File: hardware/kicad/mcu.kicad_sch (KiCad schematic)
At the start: 38 parts, among them J101 TC2050-IDC-NL, J102 UART (TX RX GND), SW101 BOOT, U101 STM32F469IIT6, Y101 8MHz CL10pF, Y102 32.768kHz CL6pF

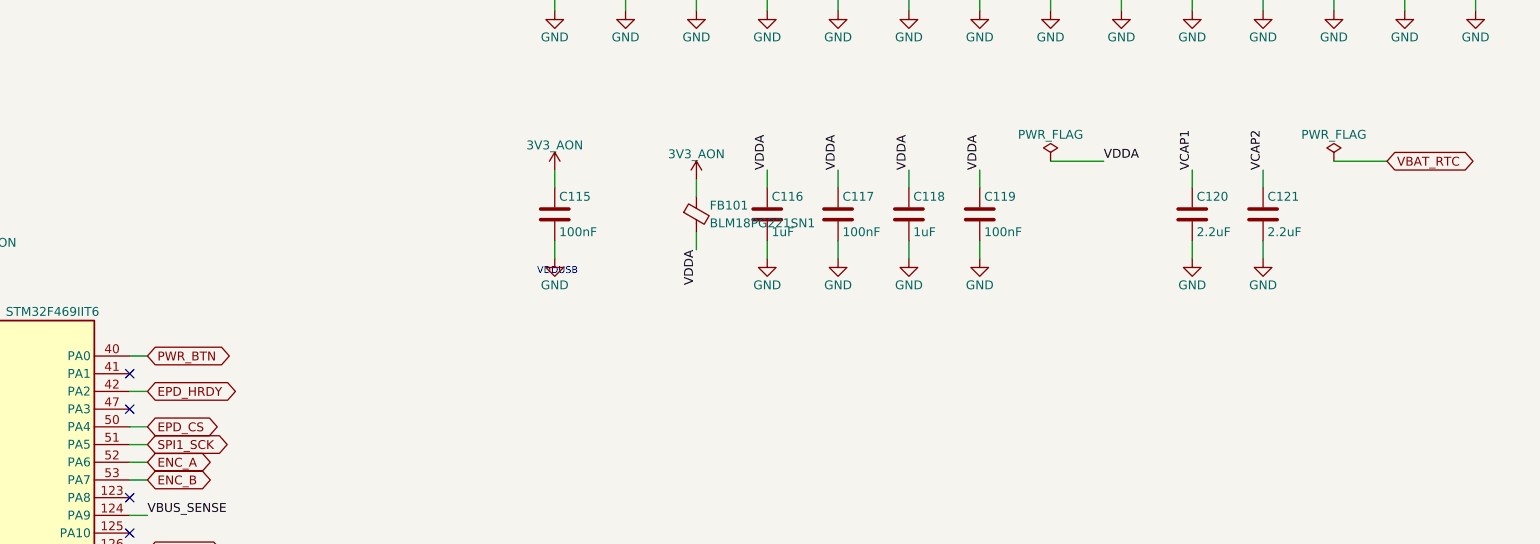
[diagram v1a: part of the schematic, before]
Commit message: Switch battery chemistry from LiFePO4 to 1-cell LiPo pouch
Small flat LFP pouches aren't practically buyable in the US; protected LiPo
pouches with JST-PH leads are stocked everywhere.

Power sheet:
- MCP73123 (3.6 V LFP) + discrete AN1149 load sharing (D1/Q1/R5) ->
  TI BQ24073: 4.2 V CV, power path with OUT (VSYS) regulated to 4.4 V so
  the 5.5 V-max TPS63802/TPS61023 stay safe, USB500 input limit, ~500 mA
  charge (ISET 1.78k), ILIM 1.54k fitted (open ILIM disables charging),
  on-board 10k NTC on TS (0-50 C charge window).
- RTC backup: BAT54J -> MCP1700 3.0 V LDO (4.2 V minus a diode drop would
  exceed VBAT's 3.6 V max).
- New VBAT_SENSE 1M/1M divider to PA3 (ADC1_IN3) for the firmware cutoff and
  fuel estimate (VBAT_RTC is now clamped by the LDO).
- UVLO divider on TPS63802 EN 1.8M/1M -> 2.2M/1M (off ~3.20 V, on ~3.52 V).
- MCP73123 project symbol removed; redundant VBAT_RTC PWR_FLAG removed.

README/TODO: chemistry rationale and trade-offs, new power tree, battery
protection layers, updated sheet notes and open items (cell choice, NTC
coupling, fitting the peripheral load switch on v1).

ERC 0 violations; check_schematic.py OK (190 nets, 84 MCU pins, 38 power-
sheet nets); PA3 pin number cross-checked against DS11189.

Co-Authored-By: Claude Opus 5.5 <noreply@anthropic.com>
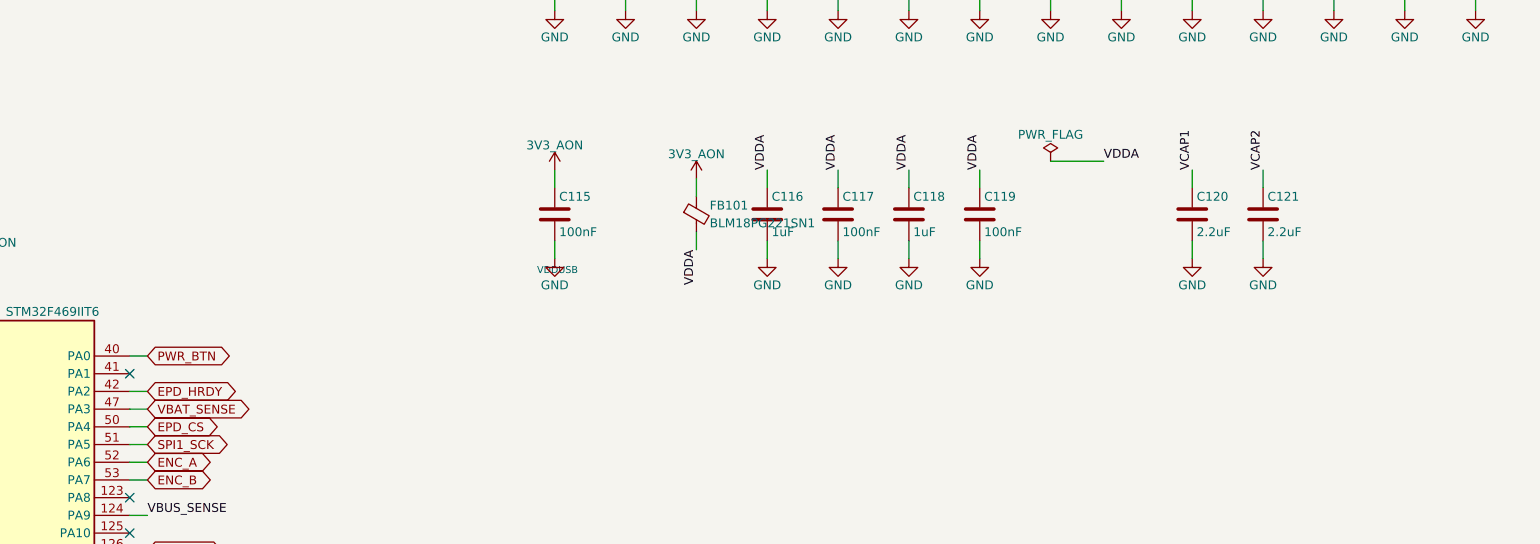
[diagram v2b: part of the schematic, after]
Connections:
- net VBAT_SENSE: now reaches U101.47 (PA3)
- no-connect marks 56 -> 55
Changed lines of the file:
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@@
 	(wire
 		(pts
+			(xy 340.36 124.46)
+			(xy 342.9 124.46)
+		)
+		(stroke
+			(width 0)
+			(type default)
+		)
+	)
+	(global_label "VBAT_SENSE"
+		(shape bidirectional)
+		(at 342.9 124.46 0)
+		(fields_autoplaced yes)
+		(effects
+			(font
+				(size 1.27 1.27)
+			)
+			(justify left)
+		)
+		(property "Intersheetrefs" "${INTERSHEET_REFS}"
+			(at 342.9 124.46 0)
+			(hide yes)
+			(effects
+				(font
+					(size 1.27 1.27)
+				)
+				(justify left)
+			)
+		)
+	)
+	(wire
+		(pts
 			(xy 254 223.52)
 			(xy 251.46 223.52)
@@
 	)
 	(no_connect
-		(at 340.36 124.46)
-	)
-	(no_connect
 		(at 340.36 213.36)
 	)
@@
 		)
 	)
-	(symbol
-		(lib_id "power:PWR_FLAG")
-		(at 513.08 88.9 0)
-		(unit 1)
-		(exclude_from_sim no)
-		(in_bom no)
-		(on_board yes)
-		(dnp no)
-		(property "Reference" "#FLGMCU49"
-			(at 513.08 86.995 0)
-			(hide yes)
-			(effects
-				(font
-					(size 1.27 1.27)
-				)
-			)
-		)
-		(property "Value" "PWR_FLAG"
-			(at 513.08 85.09 0)
-			(effects
-				(font
-					(size 1.27 1.27)
-				)
-			)
-		)
-		(property "Footprint" ""
-			(at 513.08 88.9 0)
-			(hide yes)
-			(effects
-				(font
-					(size 1.27 1.27)
-				)
-			)
-		)
-		(property "Datasheet" ""
-			(at 513.08 88.9 0)
-			(hide yes)
-			(effects
-				(font
-					(size 1.27 1.27)
-				)
-			)
-		)
-		(property "Description" "Special symbol for telling ERC where power comes from"
-			(at 513.08 88.9 0)
-			(hide yes)
-			(effects
-				(font
-					(size 1.27 1.27)
-				)
-			)
-		)
-		(pin "1"
-		)
-		(instances
-			(project "stm32-epaper"
-				(path "/6f1d3c2a-5b7e-4c1d-9a0f-000000000001/6f1d3c2a-5b7e-4c1d-9a0f-000000000004"
-					(reference "#FLGMCU49")
-					(unit 1)
-				)
-			)
-		)
-	)
-	(wire
-		(pts
-			(xy 513.08 88.9)
-			(xy 520.7 88.9)
-		)
-		(stroke
-			(width 0)
-			(type default)
-		)
-	)
-	(global_label "VBAT_RTC"
-		(shape bidirectional)
-		(at 520.7 88.9 0)
-		(fields_autoplaced yes)
-		(effects
-			(font
-				(size 1.27 1.27)
-			)
-			(justify left)
-		)
-		(property "Intersheetrefs" "${INTERSHEET_REFS}"
-			(at 520.7 88.9 0)
-			(hide yes)
-			(effects
-				(font
-					(size 1.27 1.27)
-				)
-				(justify left)
-			)
-		)
-	)
 	(text "HSE 8MHz (PLL -> 180MHz). Load caps C = 2*(CL - Cstray): for a CL = 10pF crystal\nand ~4pF stray, 12pF. LSE 32.768kHz: pick a low-CL (6-7pF) crystal the LSE\noscillator drives reliably (ST AN2867); 6.8pF shown for CL = 6pF. Verify both\nagainst the chosen crystals."
 		(exclude_from_sim no)
@@
 		(on_board yes)
 		(dnp no)
-		(property "Reference" "#PWRMCU050"
+		(property "Reference" "#PWRMCU049"
 			(at 40.64 82.55 0)
 			(hide yes)
@@
 			(project "stm32-epaper"
 				(path "/6f1d3c2a-5b7e-4c1d-9a0f-000000000001/6f1d3c2a-5b7e-4c1d-9a0f-000000000004"
-					(reference "#PWRMCU050")
+					(reference "#PWRMCU049")
 					(unit 1)
 				)
@@
 		(on_board yes)
 		(dnp no)
-		(property "Reference" "#PWRMCU051"
+		(property "Reference" "#PWRMCU050"
 			(at 40.64 82.55 0)
 			(hide yes)
@@
 			(project "stm32-epaper"
 				(path "/6f1d3c2a-5b7e-4c1d-9a0f-000000000001/6f1d3c2a-5b7e-4c1d-9a0f-000000000004"
-					(reference "#PWRMCU051")
+					(reference "#PWRMCU050")
 					(unit 1)
 				)
@@
 		(on_board yes)
 		(dnp no)
-		(property "Reference" "#PWRMCU052"
+		(property "Reference" "#PWRMCU051"
 			(at 30.48 101.6 0)
 			(hide yes)
@@
 			(project "stm32-epaper"
 				(path "/6f1d3c2a-5b7e-4c1d-9a0f-000000000001/6f1d3c2a-5b7e-4c1d-9a0f-000000000004"
-					(reference "#PWRMCU052")
+					(reference "#PWRMCU051")
 					(unit 1)
 				)
@@
 		(on_board yes)
 		(dnp no)
-		(property "Reference" "#PWRMCU053"
+		(property "Reference" "#PWRMCU052"
 			(at 50.8 101.6 0)
 			(hide yes)
@@
 			(project "stm32-epaper"
 				(path "/6f1d3c2a-5b7e-4c1d-9a0f-000000000001/6f1d3c2a-5b7e-4c1d-9a0f-000000000004"
-					(reference "#PWRMCU053")
+					(reference "#PWRMCU052")
 					(unit 1)
 				)
@@
 		(on_board yes)
 		(dnp no)
-		(property "Reference" "#PWRMCU054"
+		(property "Reference" "#PWRMCU053"
 			(at 86.36 101.6 0)
 			(hide yes)
@@
 			(project "stm32-epaper"
 				(path "/6f1d3c2a-5b7e-4c1d-9a0f-000000000001/6f1d3c2a-5b7e-4c1d-9a0f-000000000004"
-					(reference "#PWRMCU054")
+					(reference "#PWRMCU053")
 					(unit 1)
 				)
@@
 		(on_board yes)
 		(dnp no)
-		(property "Reference" "#PWRMCU055"
+		(property "Reference" "#PWRMCU054"
 			(at 106.68 101.6 0)
 			(hide yes)
@@
 			(project "stm32-epaper"
 				(path "/6f1d3c2a-5b7e-4c1d-9a0f-000000000001/6f1d3c2a-5b7e-4c1d-9a0f-000000000004"
-					(reference "#PWRMCU055")
+					(reference "#PWRMCU054")
 					(unit 1)
 				)
@@
 		(on_board yes)
 		(dnp no)
-		(property "Reference" "#PWRMCU056"
+		(property "Reference" "#PWRMCU055"
 			(at 30.48 154.94 0)
 			(hide yes)
@@
 			(project "stm32-epaper"
 				(path "/6f1d3c2a-5b7e-4c1d-9a0f-000000000001/6f1d3c2a-5b7e-4c1d-9a0f-000000000004"
-					(reference "#PWRMCU056")
+					(reference "#PWRMCU055")
 					(unit 1)
 				)
@@
 		(on_board yes)
 		(dnp no)
-		(property "Reference" "#PWRMCU057"
+		(property "Reference" "#PWRMCU056"
 			(at 50.8 154.94 0)
 			(hide yes)
@@
 			(project "stm32-epaper"
 				(path "/6f1d3c2a-5b7e-4c1d-9a0f-000000000001/6f1d3c2a-5b7e-4c1d-9a0f-000000000004"
-					(reference "#PWRMCU057")
+					(reference "#PWRMCU056")
 					(unit 1)
 				)
@@
 		(on_board yes)
 		(dnp no)
-		(property "Reference" "#PWRMCU058"
+		(property "Reference" "#PWRMCU057"
 			(at 60.96 138.43 0)
 			(hide yes)
@@
 			(project "stm32-epaper"
 				(path "/6f1d3c2a-5b7e-4c1d-9a0f-000000000001/6f1d3c2a-5b7e-4c1d-9a0f-000000000004"
-					(reference "#PWRMCU058")
+					(reference "#PWRMCU057")
 					(unit 1)
 				)
@@
 		(on_board yes)
 		(dnp no)
-		(property "Reference" "#PWRMCU059"
+		(property "Reference" "#PWRMCU058"
 			(at 96.52 154.94 0)
 			(hide yes)
@@
 			(project "stm32-epaper"
 				(path "/6f1d3c2a-5b7e-4c1d-9a0f-000000000001/6f1d3c2a-5b7e-4c1d-9a0f-000000000004"
-					(reference "#PWRMCU059")
+					(reference "#PWRMCU058")
 					(unit 1)
 				)
@@
 		(on_board yes)
 		(dnp no)
-		(property "Reference" "#PWRMCU060"
+		(property "Reference" "#PWRMCU059"
 			(at 50.8 189.23 0)
 			(hide yes)
@@
 			(project "stm32-epaper"
 				(path "/6f1d3c2a-5b7e-4c1d-9a0f-000000000001/6f1d3c2a-5b7e-4c1d-9a0f-000000000004"
-					(reference "#PWRMCU060")
+					(reference "#PWRMCU059")
 					(unit 1)
 				)
@@
 		(on_board yes)
 		(dnp no)
-		(property "Reference" "#PWRMCU061"
+		(property "Reference" "#PWRMCU060"
 			(at 50.8 227.33 0)
 			(hide yes)
@@
 			(project "stm32-epaper"
 				(path "/6f1d3c2a-5b7e-4c1d-9a0f-000000000001/6f1d3c2a-5b7e-4c1d-9a0f-000000000004"
-					(reference "#PWRMCU061")
+					(reference "#PWRMCU060")
 					(unit 1)
 				)
@@
 		(on_board yes)
 		(dnp no)
-		(property "Reference" "#PWRMCU062"
+		(property "Reference" "#PWRMCU061"
 			(at 50.8 227.33 0)
 			(hide yes)
@@
 			(project "stm32-epaper"
 				(path "/6f1d3c2a-5b7e-4c1d-9a0f-000000000001/6f1d3c2a-5b7e-4c1d-9a0f-000000000004"
-					(reference "#PWRMCU062")
+					(reference "#PWRMCU061")
 					(unit 1)
 				)
@@
 		(on_board yes)
 		(dnp no)
-		(property "Reference" "#PWRMCU063"
+		(property "Reference" "#PWRMCU062"
 			(at 40.64 257.81 0)
 			(hide yes)
@@
 			(project "stm32-epaper"
 				(path "/6f1d3c2a-5b7e-4c1d-9a0f-000000000001/6f1d3c2a-5b7e-4c1d-9a0f-000000000004"
-					(reference "#PWRMCU063")
+					(reference "#PWRMCU062")
 					(unit 1)
 				)
@@
 		(on_board yes)
 		(dnp no)
-		(property "Reference" "#PWRMCU064"
+		(property "Reference" "#PWRMCU063"
 			(at 71.12 284.48 0)
 			(hide yes)
@@
 			(project "stm32-epaper"
 				(path "/6f1d3c2a-5b7e-4c1d-9a0f-000000000001/6f1d3c2a-5b7e-4c1d-9a0f-000000000004"
-					(reference "#PWRMCU064")
+					(reference "#PWRMCU063")
 					(unit 1)
 				)
@@
 		(on_board yes)
 		(dnp no)
-		(property "Reference" "#PWRMCU065"
+		(property "Reference" "#PWRMCU064"
 			(at 46.99 303.53 0)
 			(hide yes)
@@
 			(project "stm32-epaper"
 				(path "/6f1d3c2a-5b7e-4c1d-9a0f-000000000001/6f1d3c2a-5b7e-4c1d-9a0f-000000000004"
-					(reference "#PWRMCU065")
+					(reference "#PWRMCU064")
 					(unit 1)
 				)

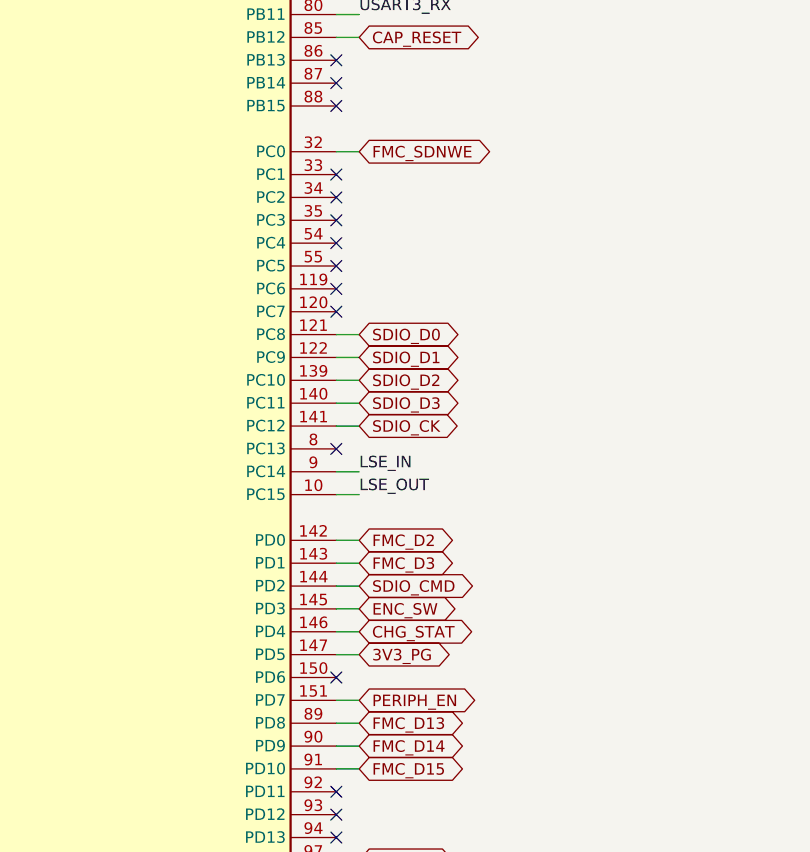
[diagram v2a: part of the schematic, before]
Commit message: Finalize charger for the chosen EEMB cells; battery bay dimensions
From EEMB's LP963450-PCM-LD pack spec and LP603449 cell spec:
- Charge current 500 mA -> ~296 mA (ISET 3.01k, 265-324 mA worst case):
  <= 0.3C of the 1100 mAh cell, EEMB's limit for charging at 0-20 C.
- TMR 72k: fast-charge timer 7.2-12 h (default 4-6 h would expire on the
  1800 mAh cell at ~300 mA).
- Cells allow charging only at 0-45 C; the BQ24073 window is ~0-50 C and TI's
  Rs/Rp network can only widen it (needs an NTC resistance ratio >= 7 across
  the window). So CE -> CHG_DIS (PD6, 100k pull-down keeps charging on with
  the MCU off) and TS -> TS_SENSE (10k/100nF to PC1, ADC1_IN11) for firmware
  supervision of the hot end.
- README: pack specs (PCM 3.0 V over-discharge / 4.28 V overcharge, 1 A
  continuous, 50 mm AWG26 leads), battery bay envelope (52 x 34.5 x 9.9 mm
  max + swelling allowance, lead exit edge), pin table. TODO: firmware
  charge-temperature supervision; arrival checks.

ERC 0 violations; check_schematic.py OK (190 nets, 86 MCU pins, 40 power-
sheet nets); PD6/PC1 pin numbers cross-checked against DS11189.

Co-Authored-By: Claude Opus 5.5 <noreply@anthropic.com>
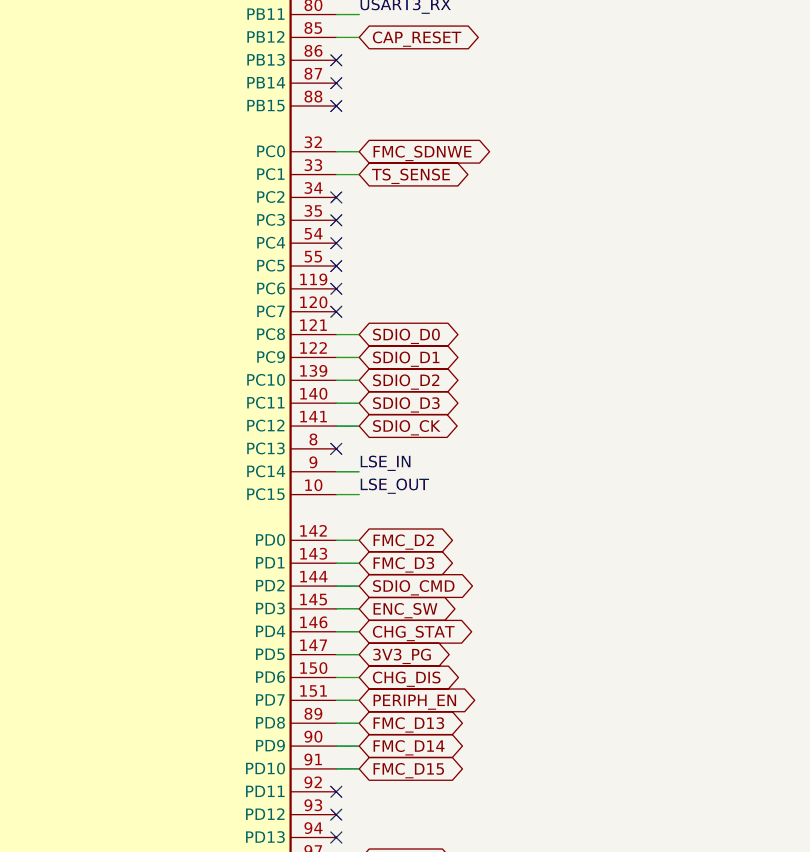
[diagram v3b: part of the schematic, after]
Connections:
- net CHG_DIS: now reaches U101.150 (PD6)
- net TS_SENSE: now reaches U101.33 (PC1)
- no-connect marks 55 -> 53
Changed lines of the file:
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@@
+	(wire
+		(pts
+			(xy 340.36 205.74)
+			(xy 342.9 205.74)
+		)
+		(stroke
+			(width 0)
+			(type default)
+		)
+	)
+	(global_label "TS_SENSE"
+		(shape bidirectional)
+		(at 342.9 205.74 0)
+		(fields_autoplaced yes)
+		(effects
+			(font
+				(size 1.27 1.27)
+			)
+			(justify left)
+		)
+		(property "Intersheetrefs" "${INTERSHEET_REFS}"
+			(at 342.9 205.74 0)
+			(hide yes)
+			(effects
+				(font
+					(size 1.27 1.27)
+				)
+				(justify left)
+			)
+		)
+	)
+	(wire
+		(pts
+			(xy 340.36 261.62)
+			(xy 342.9 261.62)
+		)
+		(stroke
+			(width 0)
+			(type default)
+		)
+	)
+	(global_label "CHG_DIS"
+		(shape bidirectional)
+		(at 342.9 261.62 0)
+		(fields_autoplaced yes)
+		(effects
+			(font
+				(size 1.27 1.27)
+			)
+			(justify left)
+		)
+		(property "Intersheetrefs" "${INTERSHEET_REFS}"
+			(at 342.9 261.62 0)
+			(hide yes)
+			(effects
+				(font
+					(size 1.27 1.27)
+				)
+				(justify left)
+			)
+		)
+	)
 	(wire
 		(pts
@@
 	)
 	(no_connect
-		(at 340.36 205.74)
-	)
-	(no_connect
 		(at 340.36 208.28)
 	)
@@
 	)
 	(no_connect
-		(at 340.36 261.62)
-	)
-	(no_connect
